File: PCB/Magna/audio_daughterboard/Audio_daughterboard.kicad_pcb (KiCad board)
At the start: 4 copper layers, 90 x 155 mm, 466 parts, among them J101 Conn_02x15_Odd_Even, J102 Conn_02x05_Odd_Even, J1301 Conn_01x03_Pin, J1302 Conn_ARM_SWD_TagConnect_TC2030, J1303 Conn_01x02_Pin, J1304 Conn_01x02_Pin, J201 PSG01550, J301 PSG01550, J601 PSG01550, Q601 NMOS, Q602 NMOS, U1001 NE5532, U1002 NE5532, U1003 NE5532, U1004 NE5532, U1005 LM1971M, U101 CY2305SXC-1HT, U102 CY2305SXC-1HT, U1101 NE5532, U1102 NE5532, U1103 NE5532, U1104 NE5532, U1105 LM1971M, U1201 NE5532, U1202 NE5532, U1203 NE5532, U1204 NE5532, U1205 LM1971M, U1301 STM32F030C8Tx, U201 WM8782SEDS, U301 WM8782SEDS, U401 PCM1789, U402 NE5532, U403 NE5532, U501 PCM1789, U502 NE5532, U503 NE5532, U601 NE5532, U701 NE5532, U801 TLV61046ADBVR, U802 LM350_TO263-3, U803 LM350_TO263-3, U901 NE5532, U902 NE5532, U903 NE5532, U904 NE5532, U905 LM1971M

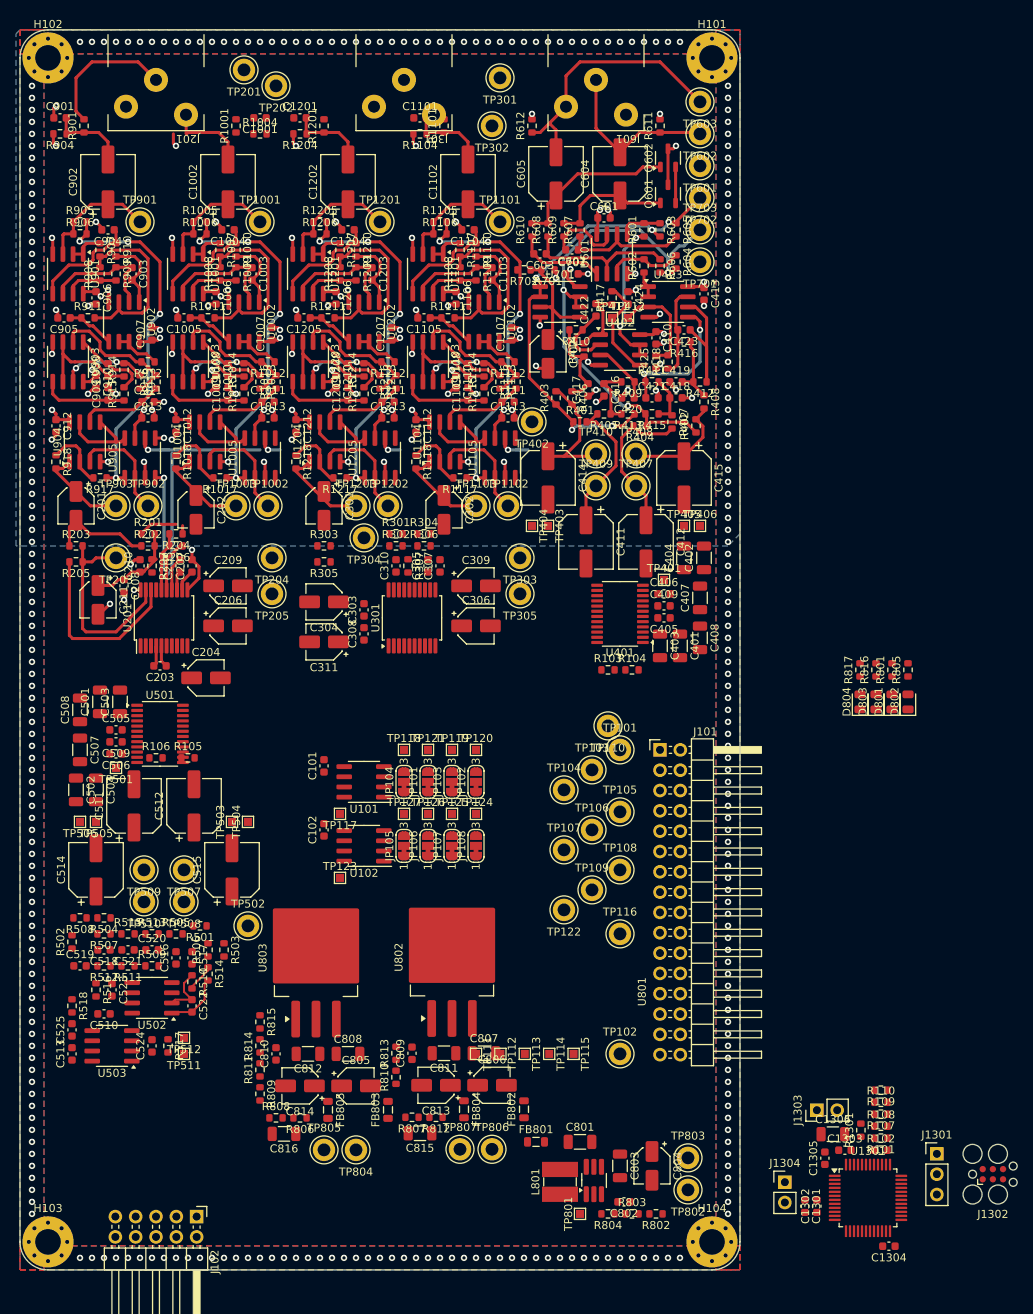
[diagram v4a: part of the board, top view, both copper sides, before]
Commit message: Finished first round of routing for the Audio Daughterboard
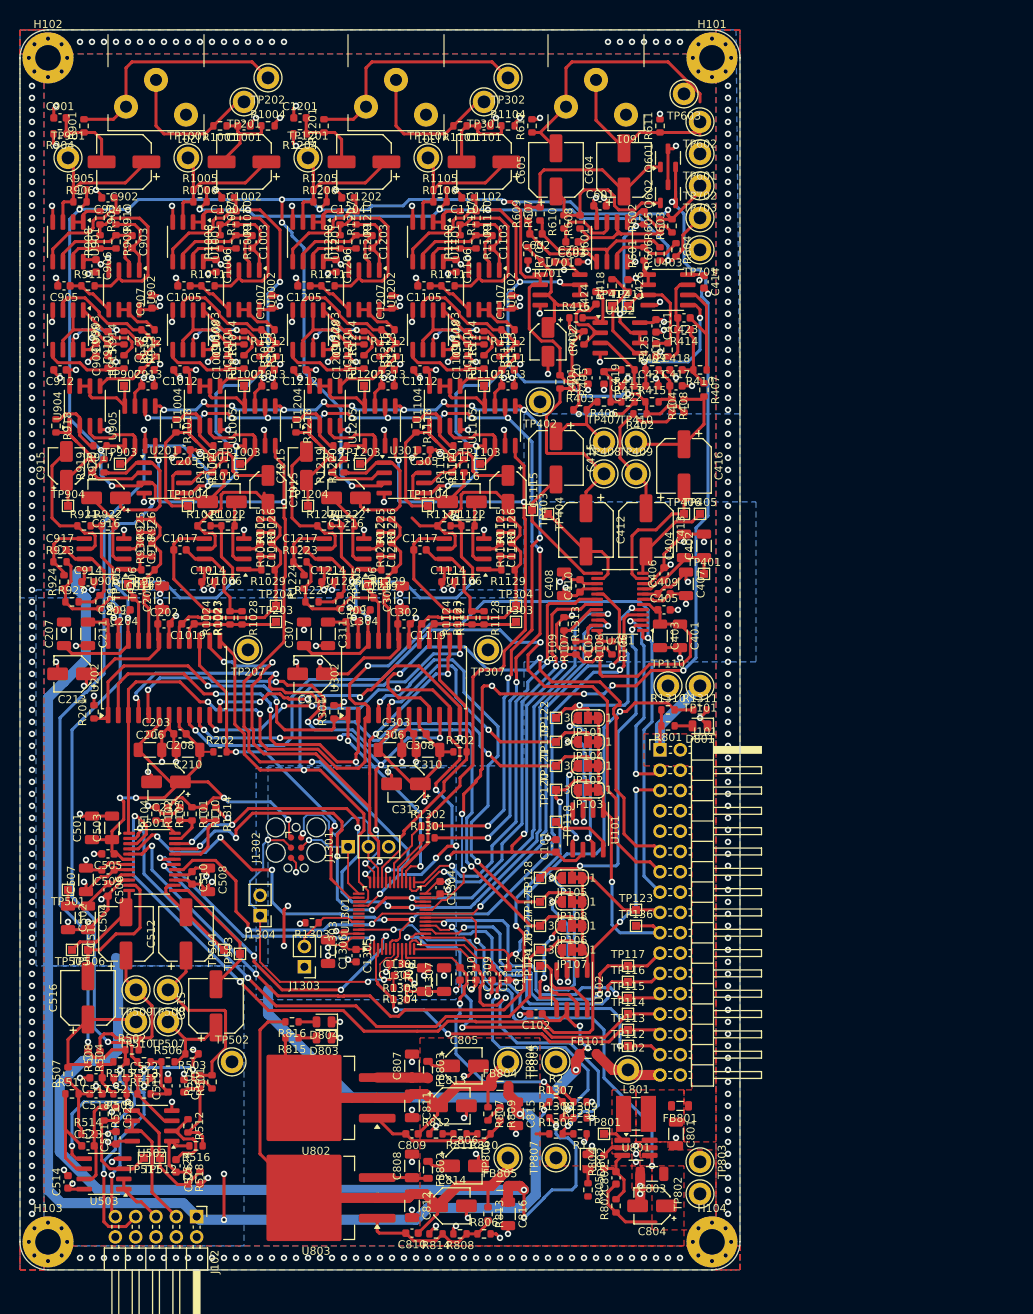
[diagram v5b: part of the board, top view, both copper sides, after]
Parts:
- removed the FB805 at (38.5, 135.0)
- removed R203, R204, R205, R206, R303, R304, R305, R306: 1k, Resistor_SMD:R_0603_1608Metric
- removed R207, R307: 2k15, Resistor_SMD:R_0603_1608Metric
- removed R803: 22k, Resistor_SMD:R_0603_1608Metric
- removed the R808 at (32.0, 136.0)
- removed the R809 at (30.0, 133.0)
- removed the R815 at (30.0, 124.0)
- removed TP103, TP104, TP105, TP106, TP107, TP108, TP109: TestPoint, TestPoint:TestPoint_Keystone_5005-5009_Compact
- removed the TP116 at (75.0, 113.0)
- removed the TP122 at (68.0, 110.0)
- added C1014: 100nF, Capacitor_SMD:C_0603_1608Metric, F.Cu at (23.5, 69.0)
- added C1015: 10uF, Capacitor_SMD:CP_Elec_4x5.8, F.Cu at (31.0, 57.5)
- added C1016: 10uF, Capacitor_SMD:CP_Elec_4x5.8, F.Cu at (25.2, 59.0)
- added C1017: 470p, Capacitor_SMD:C_0603_1608Metric, F.Cu at (20.0, 65.0)
- added C1018: 470p, Capacitor_SMD:C_0603_1608Metric, F.Cu at (30.0, 65.0)
- added C1019: 2.7n, Capacitor_SMD:C_0603_1608Metric, F.Cu at (21.0, 74.2)
- added C1114: 100nF, Capacitor_SMD:C_0603_1608Metric, F.Cu at (53.5, 69.0)
- added C1115: 10uF, Capacitor_SMD:CP_Elec_4x5.8, F.Cu at (61.0, 57.5)
- added C1116: 10uF, Capacitor_SMD:CP_Elec_4x5.8, F.Cu at (55.2, 59.0)
- added C1117: 470p, Capacitor_SMD:C_0603_1608Metric, F.Cu at (50.0, 65.0)
- added C1118: 470p, Capacitor_SMD:C_0603_1608Metric, F.Cu at (60.0, 65.0)
- added C1119: 2.7n, Capacitor_SMD:C_0603_1608Metric, F.Cu at (51.0, 74.2)
- added C1214: 100nF, Capacitor_SMD:C_0603_1608Metric, F.Cu at (38.5, 69.0)
- added C1215: 10uF, Capacitor_SMD:CP_Elec_4x5.8, F.Cu at (35.8, 54.5)
- added C1216: 10uF, Capacitor_SMD:CP_Elec_4x5.8, F.Cu at (40.8, 58.5)
- added C1217: 470p, Capacitor_SMD:C_0603_1608Metric, F.Cu at (35.0, 65.0)
- added C1218: 470p, Capacitor_SMD:C_0603_1608Metric, F.Cu at (45.0, 65.0)
- added C1219: 2.7n, Capacitor_SMD:C_0603_1608Metric, F.Cu at (45.0, 71.0)
- added C1307: 4.7uF, Capacitor_SMD:C_1206_3216Metric, F.Cu at (53.0, 118.7)
- added C1308: 4.7uF, Capacitor_SMD:C_1206_3216Metric, F.Cu at (50.5, 118.7)
- added C1309: 100nF, Capacitor_SMD:C_0603_1608Metric, F.Cu at (57.0, 118.0)
- added C1310: 100nF, Capacitor_SMD:C_0603_1608Metric, F.Cu at (55.0, 118.0)
- added C1311: 100nF, Capacitor_SMD:C_0603_1608Metric, F.Cu at (59.0, 118.0)
- added C1312: 100nF, Capacitor_SMD:C_0603_1608Metric, F.Cu at (61.0, 118.0)
- added C212: 10uF, Capacitor_SMD:CP_Elec_4x5.8, F.Cu at (18.2, 94.0)
- added C213: 10uF, Capacitor_SMD:CP_Elec_4x5.8, F.Cu at (6.50, 80.5)
- added C312: 10uF, Capacitor_SMD:CP_Elec_4x5.8, F.Cu at (48.2, 94.2)
- added C313: 10uF, Capacitor_SMD:CP_Elec_4x5.8, F.Cu at (36.5, 80.5)
- added C410: 100nF, Capacitor_SMD:C_0603_1608Metric, F.Cu at (70.0, 69.5)
- added C510: 100nF, Capacitor_SMD:C_0603_1608Metric, F.Cu at (21.5, 106.0)
- added C914: 100nF, Capacitor_SMD:C_0603_1608Metric, F.Cu at (8.50, 69.0)
- added C915: 10uF, Capacitor_SMD:CP_Elec_4x5.8, F.Cu at (5.80, 54.5)
- added C916: 10uF, Capacitor_SMD:CP_Elec_4x5.8, F.Cu at (10.8, 58.5)
- added C917: 470p, Capacitor_SMD:C_0603_1608Metric, F.Cu at (5.00, 65.0)
- added C918: 470p, Capacitor_SMD:C_0603_1608Metric, F.Cu at (15.0, 65.0)
- added C919: 2.7n, Capacitor_SMD:C_0603_1608Metric, F.Cu at (15.0, 71.0)
- added FB101: FerriteBead, Inductor_SMD:L_0805_2012Metric, F.Cu at (71.0, 128.0)
- added FB804: FerriteBead, Inductor_SMD:L_0805_2012Metric, F.Cu at (60.0, 132.0)
- added R1: 2k15, Resistor_SMD:R_0603_1608Metric, F.Cu at (70.0, 138.0)
- added R1019: 1k, Resistor_SMD:R_0603_1608Metric, F.Cu at (24.0, 54.5)
- added R1020: 1k, Resistor_SMD:R_0603_1608Metric, F.Cu at (25.5, 54.5)
- added R1021: 10k, Resistor_SMD:R_0603_1608Metric, F.Cu at (23.0, 62.0)
- added R1022: 10k, Resistor_SMD:R_0603_1608Metric, F.Cu at (26.0, 62.0)
- added R1023: 10k, Resistor_SMD:R_0603_1608Metric, F.Cu at (23.2, 73.5)
- added R1024: 680R, Resistor_SMD:R_0603_1608Metric, F.Cu at (24.8, 73.5)
- added R1025: 10k, Resistor_SMD:R_0603_1608Metric, F.Cu at (31.5, 62.0)
- added R1026: 680R, Resistor_SMD:R_0603_1608Metric, F.Cu at (30.0, 62.0)
- added R1027: 100R, Resistor_SMD:R_0603_1608Metric, F.Cu at (26.2, 73.5)
- added R1028: 1k, Resistor_SMD:R_0603_1608Metric, F.Cu at (27.8, 73.5)
- added R1029: 100R, Resistor_SMD:R_0603_1608Metric, F.Cu at (31.0, 67.5)
- added R1030: 1k, Resistor_SMD:R_0603_1608Metric, F.Cu at (31.5, 65.0)
- added R1119: 1k, Resistor_SMD:R_0603_1608Metric, F.Cu at (54.0, 54.5)
- added R1120: 1k, Resistor_SMD:R_0603_1608Metric, F.Cu at (55.5, 54.5)
- added R1121: 10k, Resistor_SMD:R_0603_1608Metric, F.Cu at (53.0, 62.0)
- added R1122: 10k, Resistor_SMD:R_0603_1608Metric, F.Cu at (56.0, 62.0)
- added R1123: 10k, Resistor_SMD:R_0603_1608Metric, F.Cu at (53.2, 73.5)
- added R1124: 680R, Resistor_SMD:R_0603_1608Metric, F.Cu at (54.8, 73.5)
- added R1125: 10k, Resistor_SMD:R_0603_1608Metric, F.Cu at (61.5, 62.0)
- added R1126: 680R, Resistor_SMD:R_0603_1608Metric, F.Cu at (60.0, 62.0)
- added R1127: 100R, Resistor_SMD:R_0603_1608Metric, F.Cu at (56.5, 73.5)
- added R1128: 1k, Resistor_SMD:R_0603_1608Metric, F.Cu at (58.0, 73.5)
- added R1129: 100R, Resistor_SMD:R_0603_1608Metric, F.Cu at (61.0, 67.5)
- added R1130: 1k, Resistor_SMD:R_0603_1608Metric, F.Cu at (61.5, 65.0)
- added R1219: 1k, Resistor_SMD:R_0603_1608Metric, F.Cu at (39.0, 54.5)
- added R1220: 1k, Resistor_SMD:R_0603_1608Metric, F.Cu at (40.5, 54.5)
- added R1221: 10k, Resistor_SMD:R_0603_1608Metric, F.Cu at (38.0, 62.0)
- added R1222: 10k, Resistor_SMD:R_0603_1608Metric, F.Cu at (41.0, 62.0)
- added R1223: 10k, Resistor_SMD:R_0603_1608Metric, F.Cu at (35.0, 66.5)
- added R1224: 680R, Resistor_SMD:R_0603_1608Metric, F.Cu at (35.5, 69.0)
- added R1225: 10k, Resistor_SMD:R_0603_1608Metric, F.Cu at (46.5, 62.0)
- added R1226: 680R, Resistor_SMD:R_0603_1608Metric, F.Cu at (45.0, 62.0)
- added R1227: 100R, Resistor_SMD:R_0603_1608Metric, F.Cu at (36.5, 71.5)
- added R1228: 1k, Resistor_SMD:R_0603_1608Metric, F.Cu at (40.0, 71.5)
- added R1229: 100R, Resistor_SMD:R_0603_1608Metric, F.Cu at (46.0, 67.5)
- added R1230: 1k, Resistor_SMD:R_0603_1608Metric, F.Cu at (46.5, 65.0)
- added R1231: 1k, Resistor_SMD:R_0603_1608Metric, F.Cu at (70.0, 134.0)
- added R1301: 68R, Resistor_SMD:R_0603_1608Metric, F.Cu at (51.0, 101.0)
- added R1302: 68R, Resistor_SMD:R_0603_1608Metric, F.Cu at (51.0, 99.5)
- added R1304: 10k, Resistor_SMD:R_0603_1608Metric, F.Cu at (47.5, 119.7)
- added R1305: 10k, Resistor_SMD:R_0603_1608Metric, F.Cu at (47.5, 121.2)
- added R1306: 10k, Resistor_SMD:R_0603_1608Metric, F.Cu at (67.0, 138.0)
- added R1307: 10k, Resistor_SMD:R_0603_1608Metric, F.Cu at (67.0, 134.0)
- added R1308: 10k, Resistor_SMD:R_0603_1608Metric, F.Cu at (67.0, 136.0)
- added R1309: 10k, Resistor_SMD:R_0603_1608Metric, F.Cu at (70.0, 136.0)
- added R1310: 10k, Resistor_SMD:R_0603_1608Metric, F.Cu at (81.0, 85.0)
- added R1311: 10k, Resistor_SMD:R_0603_1608Metric, F.Cu at (85.0, 85.0)
- added R1313: 68R, Resistor_SMD:R_0603_1608Metric, F.Cu at (68.0, 74.2)
- added R1314: 68R, Resistor_SMD:R_0603_1608Metric, F.Cu at (24.5, 98.0)
- added R2: 1k96, Resistor_SMD:R_0603_1608Metric, F.Cu at (67.0, 132.5)
- added R811: 1k96, Resistor_SMD:R_0603_1608Metric, F.Cu at (55.0, 138.0)
- added R812: 1k, Resistor_SMD:R_0603_1608Metric, F.Cu at (52.0, 138.0)
- added R919: 1k, Resistor_SMD:R_0603_1608Metric, F.Cu at (9.00, 54.5)
- added R920: 1k, Resistor_SMD:R_0603_1608Metric, F.Cu at (10.5, 54.5)
- added R921: 10k, Resistor_SMD:R_0603_1608Metric, F.Cu at (8.00, 62.0)
- added R922: 10k, Resistor_SMD:R_0603_1608Metric, F.Cu at (11.0, 62.0)
- added R923: 10k, Resistor_SMD:R_0603_1608Metric, F.Cu at (5.00, 66.5)
- added R924: 680R, Resistor_SMD:R_0603_1608Metric, F.Cu at (5.50, 69.0)
- added R925: 10k, Resistor_SMD:R_0603_1608Metric, F.Cu at (16.5, 62.0)
- added R926: 680R, Resistor_SMD:R_0603_1608Metric, F.Cu at (15.0, 62.0)
- added R927: 100R, Resistor_SMD:R_0603_1608Metric, F.Cu at (6.50, 71.5)
- added R928: 1k, Resistor_SMD:R_0603_1608Metric, F.Cu at (10.0, 71.5)
- added R929: 100R, Resistor_SMD:R_0603_1608Metric, F.Cu at (16.0, 67.5)
- added R930: 1k, Resistor_SMD:R_0603_1608Metric, F.Cu at (16.5, 65.0)
- added TP1004: TestPoint, TestPoint:TestPoint_Pad_1.0x1.0mm, F.Cu at (21.0, 59.5)
- added TP1104: TestPoint, TestPoint:TestPoint_Pad_1.0x1.0mm, F.Cu at (51.0, 59.5)
- added TP112: TestPoint, TestPoint:TestPoint_Pad_1.0x1.0mm, F.Cu at (76.0, 127.0)
- added TP1204: TestPoint, TestPoint:TestPoint_Pad_1.0x1.0mm, F.Cu at (36.0, 59.5)
- added TP123: TestPoint, TestPoint:TestPoint_Pad_1.0x1.0mm, F.Cu at (77.0, 110.0)
- added TP136: TestPoint, TestPoint:TestPoint_Pad_1.0x1.0mm, F.Cu at (77.0, 112.0)
- added TP205: TestPoint, TestPoint:TestPoint_Pad_1.0x1.0mm, F.Cu at (13.5, 69.2)
- added TP206: TestPoint, TestPoint:TestPoint_Pad_1.0x1.0mm, F.Cu at (15.5, 69.2)
- added TP305: TestPoint, TestPoint:TestPoint_Pad_1.0x1.0mm, F.Cu at (43.5, 69.2)
- added TP306: TestPoint, TestPoint:TestPoint_Pad_1.0x1.0mm, F.Cu at (45.5, 69.2)
- added TP904: TestPoint, TestPoint:TestPoint_Pad_1.0x1.0mm, F.Cu at (6.00, 59.5)
- added U1006: NE5532, Package_SO:SOIC-8_3.9x4.9mm_P1.27mm, F.Cu at (25.5, 65.5)
- added U1106: NE5532, Package_SO:SOIC-8_3.9x4.9mm_P1.27mm, F.Cu at (55.5, 65.5)
- added U1206: NE5532, Package_SO:SOIC-8_3.9x4.9mm_P1.27mm, F.Cu at (40.5, 65.5)
- added U202: CS5361, Package_SO:SOIC-24W_7.5x15.4mm_P1.27mm, F.Cu at (18.0, 81.0)
- added U302: CS5361, Package_SO:SOIC-24W_7.5x15.4mm_P1.27mm, F.Cu at (48.0, 81.0)
- added U906: NE5532, Package_SO:SOIC-8_3.9x4.9mm_P1.27mm, F.Cu at (10.5, 65.5)
- C201, C206, C211, C301, C306, C311: value 10uF -> 4.7uF; footprint Capacitor_SMD:CP_Elec_4x5.8 -> Capacitor_SMD:C_1206_3216Metric
- C202, C204, C209, C302, C304, C309: value 10uF -> 100nF; footprint Capacitor_SMD:CP_Elec_4x5.8 -> Capacitor_SMD:C_0603_1608Metric
- C207, C210, C307, C310: value 100nF -> 4.7uF; footprint Capacitor_SMD:C_0603_1608Metric -> Capacitor_SMD:C_1206_3216Metric
- J101: footprint Connector_PinHeader_2.54mm:PinHeader_2x16_P2.54mm_Horizontal -> Connector_PinHeader_2.54mm:PinHeader_2x17_P2.54mm_Horizontal
- R201, R202, R301, R302: value 100k -> 10k
- TP1002, TP1003, TP1102, TP1103, TP1202, TP1203, TP203, TP204, TP303, TP304, TP902, TP903: footprint TestPoint:TestPoint_Keystone_5005-5009_Compact -> TestPoint:TestPoint_Pad_1.0x1.0mm
- U201, U301: value WM8782SEDS -> NE5532; footprint Package_SO:SSOP-20_5.3x7.2mm_P0.65mm -> Package_SO:SOIC-8_3.9x4.9mm_P1.27mm
- moved R102 97.2 mm to (20.0, 98.0), turned to 90 degrees
- moved J1302 96.2 mm to (34.5, 102.2), turned to -90 degrees
- moved R101 95.2 mm to (21.5, 98.0), turned to -90 degrees
- moved R110 92.0 mm to (23.0, 98.0), turned to -90 degrees
- moved R816 85.2 mm to (34.0, 124.0), turned to 180 degrees
- moved R815 84.6 mm to (34.0, 126.0), turned to 180 degrees
- moved J1301 83.0 mm to (41.0, 102.1), turned to 90 degrees
- moved D804 79.8 mm to (38.0, 124.0), turned to 180 degrees
- moved D803 79.1 mm to (38.0, 126.0), turned to 180 degrees
- moved R805 76.3 mm to (71.0, 145.0), turned to -90 degrees
- moved J1304 73.6 mm to (30.0, 110.7), turned to 180 degrees
- moved R1303 73.3 mm to (36.5, 111.6), turned to 180 degrees
- moved C1304 71.8 mm to (52.5, 107.2), turned to -90 degrees
- moved R108 70.1 mm to (71.0, 77.2), turned to -90 degrees
- moved D802 70.0 mm to (71.0, 141.5), turned to -90 degrees
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- renumbered C410 to C411, C411 to C412, C412 to C413, C413 to C414, C414 to C415, C415 to C416, C416 to C417, C417 to C418, C418 to C419, C419 to C420, C420 to C421, C421 to C422, C422 to C423, C423 to C424, C424 to C425, C425 to C426, C510 to C511, C511 to C512, C512 to C513, C513 to C514, C514 to C515, C515 to C516, C516 to C517, C517 to C518, C518 to C519, C519 to C520, C520 to C521, C521 to C522, C522 to C523, C523 to C524, C524 to C525, C525 to C526, C808 to C807, C807 to C808, C810 to C809, C809 to C810, C812 to C811, C811 to C812, C814 to C813, C813 to C814, C816 to C815, C815 to C816, D804 to D803, D803 to D804, FB804 to FB805, R1301 to R1303, R807 to R806, R806 to R807, R810 to R808, R811 to R809, R814 to R810, R812 to R813, R813 to R814, R817 to R815, TP111 to TP113, TP112 to TP114, TP113 to TP115, TP114 to TP116, TP115 to TP117, TP117 to TP118, TP118 to TP119, TP119 to TP120, TP120 to TP121, TP121 to TP122, TP123 to TP124, TP124 to TP125, TP125 to TP126, TP126 to TP127, TP127 to TP128, TP205 to TP207, TP305 to TP307, U403 to U402, U402 to U403, U503 to U502, U502 to U503, U803 to U802, U802 to U803
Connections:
- net /AudioPower/14.5VAA renamed /AudioPower/12VAA
- net /AudioPower/16V renamed 14V
- C1008 pad 1: Net-(U1003A-+) -> Net-(U1003A--)
- C1011 pad 1: Net-(U1004B--) -> Net-(U1004B-+)
- C1108 pad 1: Net-(U1103A-+) -> Net-(U1103A--)
- C1111 pad 1: Net-(U1104B--) -> Net-(U1104B-+)
- C1208 pad 1: Net-(U1203A-+) -> Net-(U1203A--)
- C1211 pad 1: Net-(U1204B--) -> Net-(U1204B-+)
- C1301 pad 1: /CFG_AUDIO_ENA -> /Config MCU/MCU_NRST
- C201 pad 1: /AudioAdc0/Input Filtering/signal_out -> +5VA
- C201 pad 2: Net-(C201-Pad2) -> GND
- C202 pad 1: /AudioAdc0/Input Filtering1/signal_out -> +5VA
- C202 pad 2: Net-(C202-Pad2) -> GND
- C204 pad 1: VDD -> /AudioAdc0/VQ
- C205 pad 1: +5VA -> VAA
- C206 pad 1: +5VA -> VDD
- C207 pad 1: Net-(U201-VREFP) -> /AudioAdc0/VQ
- C208 pad 1: /AudioAdc0/VMID -> VDD
- C209 pad 1: Net-(U201-VREFP) -> Net-(U202-FILT+)
- C210 pad 1: /AudioAdc0/VMID -> VDD
- C211 pad 1: /AudioAdc0/VMID -> Net-(U202-FILT+)
- C301 pad 1: /AudioAdc1/Input Filtering/signal_out -> +5VA
- C301 pad 2: Net-(C301-Pad2) -> GND
- C302 pad 1: /AudioAdc1/Input Filtering1/signal_out -> +5VA
- C302 pad 2: Net-(C302-Pad2) -> GND
- C304 pad 1: VDD -> /AudioAdc1/VQ
- C305 pad 1: +5VA -> VAA
- C306 pad 1: +5VA -> VDD
- C307 pad 1: Net-(U301-VREFP) -> /AudioAdc1/VQ
- C308 pad 1: /AudioAdc1/VMID -> VDD
- C309 pad 1: Net-(U301-VREFP) -> Net-(U302-FILT+)
- C310 pad 1: /AudioAdc1/VMID -> VDD
- C311 pad 1: /AudioAdc1/VMID -> Net-(U302-FILT+)
- C412 pad 1: /AudioDac0/VOUTL+_BIASED -> /AudioDac0/VOUTR-_BIASED
- C412 pad 2: /AudioDac0/VOUTL+ -> /AudioDac0/VOUTR-
- C413 pad 1: /AudioDac0/VOUTR+_BIASED -> /AudioDac0/VOUTL+_BIASED
- C413 pad 2: /AudioDac0/VOUTR+ -> /AudioDac0/VOUTL+
- C415 pad 1: /AudioDac0/VOUTL-_BIASED -> /AudioDac0/VOUTR+_BIASED
- C415 pad 2: /AudioDac0/VOUTL- -> /AudioDac0/VOUTR+
- C416 pad 1: /AudioDac0/VOUTR-_BIASED -> /AudioDac0/VOUTL-_BIASED
- C416 pad 2: /AudioDac0/VOUTR- -> /AudioDac0/VOUTL-
- C417 pad 1: Net-(C416-Pad1) -> Net-(C417-Pad1)
- C418 pad 2: Net-(C417-Pad2) -> Net-(C418-Pad2)
- C419 pad 1: Net-(C418-Pad1) -> Net-(C419-Pad1)
- C420 pad 2: Net-(C419-Pad2) -> Net-(C420-Pad2)
- C421 pad 1: Net-(U402A-+) -> Net-(U403B-+)
- C422 pad 1: Net-(U403B-+) -> Net-(U402A-+)
- C423 pad 1: Net-(U402A--) -> Net-(U403B--)
- C423 pad 2: Net-(C422-Pad2) -> Net-(C423-Pad2)
- C424 pad 1: Net-(U403B--) -> Net-(U402A--)
- C424 pad 2: Net-(C423-Pad2) -> Net-(C424-Pad2)
- C512 pad 1: /AudioDac1/VOUTL+_BIASED -> /AudioDac1/VOUTR-_BIASED
- C512 pad 2: /AudioDac1/VOUTL+ -> /AudioDac1/VOUTR-
- C513 pad 1: /AudioDac1/VOUTR+_BIASED -> /AudioDac1/VOUTL+_BIASED
- C513 pad 2: /AudioDac1/VOUTR+ -> /AudioDac1/VOUTL+
- C515 pad 1: /AudioDac1/VOUTL-_BIASED -> /AudioDac1/VOUTR+_BIASED
- C515 pad 2: /AudioDac1/VOUTL- -> /AudioDac1/VOUTR+
- C516 pad 1: /AudioDac1/VOUTR-_BIASED -> /AudioDac1/VOUTL-_BIASED
- C516 pad 2: /AudioDac1/VOUTR- -> /AudioDac1/VOUTL-
- C517 pad 1: Net-(C516-Pad1) -> Net-(C517-Pad1)
- C518 pad 2: Net-(C517-Pad2) -> Net-(C518-Pad2)
- C519 pad 1: Net-(C518-Pad1) -> Net-(C519-Pad1)
- C520 pad 2: Net-(C519-Pad2) -> Net-(C520-Pad2)
- C521 pad 1: Net-(U502A-+) -> Net-(U503B-+)
- C522 pad 1: Net-(U503B-+) -> Net-(U502A-+)
- C523 pad 1: Net-(U502A--) -> Net-(U503B--)
- C523 pad 2: Net-(C522-Pad2) -> Net-(C523-Pad2)
- C524 pad 1: Net-(U503B--) -> Net-(U502A--)
- C524 pad 2: Net-(C523-Pad2) -> Net-(C524-Pad2)
- C602 pad 1: Net-(U601B--) -> Net-(U601A--)
- C603 pad 1: Net-(U601A--) -> Net-(U601B--)
- C908 pad 1: Net-(U903A-+) -> Net-(U903A--)
- C911 pad 1: Net-(U904B--) -> Net-(U904B-+)
- J101 pad 31: VDD -> /AUDIO_CFG_INT
- J102 pad 3: /AudioDac1/OUT_L -> /AudioDac1/OUT_R
- J102 pad 5: /AudioDac1/OUT_R -> /AudioDac1/OUT_L
- J1302 pad 3: /CFG_AUDIO_ENA -> /Config MCU/MCU_NRST
- J1304 pad 1: /CFG_AUDIO_ENA -> /Config MCU/MCU_NRST
- J201 pad 1: /AudioAdc0/Input Filtering/signal in -> /AudioAdc0/Input Filtering1/signal in
- J201 pad 2: /AudioAdc0/Input Filtering1/signal in -> /AudioAdc0/Input Filtering/signal in
- J301 pad 1: /AudioAdc1/Input Filtering/signal in -> /AudioAdc1/Input Filtering1/signal in
- J301 pad 2: /AudioAdc1/Input Filtering1/signal in -> /AudioAdc1/Input Filtering/signal in
- JP102 pad 2: /DAC0_MCLK -> /ADC0_MCLK
- JP103 pad 2: /ADC1_MCLK -> /DAC0_MCLK
- JP104 pad 2: /ADC0_MCLK -> /ADC1_MCLK
- JP106 pad 2: /DAC0_BCLK -> /ADC0_BCLK
- JP107 pad 2: /ADC1_BCLK -> /DAC0_BCLK
- JP108 pad 2: /ADC0_BCLK -> /ADC1_BCLK
- Q601 pad 2: MASTER_MUTE -> /Config MCU/LINE_MUTE
- Q602 pad 2: MASTER_MUTE -> /Config MCU/LINE_MUTE
- R1005 pad 2: VAA_BIAS_R -> VAA_BIAS_L
- R1006 pad 2: VAA_BIAS_R -> VAA_BIAS_L
- R1012 pad 2: Net-(U1003A--) -> Net-(U1003A-+)
- R1013 pad 2: Net-(U1003A--) -> Net-(U1003A-+)
- R1014 pad 1: Net-(U1003A-+) -> Net-(U1003A--)
- R1016 pad 1: Net-(U1004B--) -> Net-(U1004B-+)
- R1016 pad 2: Net-(U1003A--) -> Net-(U1003A-+)
- R1017 pad 1: VAA_BIAS_R -> VAA_BIAS_L
- R1018 pad 2: /AudioAdc0/Input Filtering1/signal_out -> Net-(C1015-Pad1)
- R110 pad 1: /AudioDac0/MODE -> VDD
- R110 pad 2: GND -> /AudioDac1/MODE
- R1105 pad 2: VAA_BIAS_R -> VAA_BIAS_L
- R1106 pad 2: VAA_BIAS_R -> VAA_BIAS_L
- R1112 pad 2: Net-(U1103A--) -> Net-(U1103A-+)
- R1113 pad 2: Net-(U1103A--) -> Net-(U1103A-+)
- R1114 pad 1: Net-(U1103A-+) -> Net-(U1103A--)
- R1116 pad 1: Net-(U1104B--) -> Net-(U1104B-+)
- R1116 pad 2: Net-(U1103A--) -> Net-(U1103A-+)
- R1117 pad 1: VAA_BIAS_R -> VAA_BIAS_L
- R1118 pad 2: /AudioAdc1/Input Filtering1/signal_out -> Net-(C1115-Pad1)
- R1205 pad 2: VAA_BIAS_L -> VAA_BIAS_R
- R1206 pad 2: VAA_BIAS_L -> VAA_BIAS_R
- R1212 pad 2: Net-(U1203A--) -> Net-(U1203A-+)
- R1213 pad 2: Net-(U1203A--) -> Net-(U1203A-+)
- R1214 pad 1: Net-(U1203A-+) -> Net-(U1203A--)
- R1216 pad 1: Net-(U1204B--) -> Net-(U1204B-+)
- R1216 pad 2: Net-(U1203A--) -> Net-(U1203A-+)
- R1217 pad 1: VAA_BIAS_L -> VAA_BIAS_R
- R1218 pad 2: /AudioAdc1/Input Filtering/signal_out -> Net-(C1215-Pad1)
- R201 pad 1: Net-(C202-Pad2) -> /AudioAdc0/ADC_RST
- R201 pad 2: /AudioAdc0/VMID -> GND
- R202 pad 1: Net-(C201-Pad2) -> VDD
- R202 pad 2: /AudioAdc0/VMID -> /AudioAdc0/ADC_OVFL
- R301 pad 1: Net-(C302-Pad2) -> /AudioAdc0/ADC_RST
- R301 pad 2: /AudioAdc1/VMID -> GND
- R302 pad 1: Net-(C301-Pad2) -> VDD
- R302 pad 2: /AudioAdc1/VMID -> /AudioAdc1/ADC_OVFL
- R401 pad 1: VAA_BIAS_L -> VAA_BIAS_R
- R401 pad 2: /AudioDac0/VOUTL+_BIASED -> /AudioDac0/VOUTR-_BIASED
- R402 pad 1: VAA_BIAS_R -> VAA_BIAS_L
- R402 pad 2: /AudioDac0/VOUTR-_BIASED -> /AudioDac0/VOUTL+_BIASED
- R403 pad 1: VAA_BIAS_L -> VAA_BIAS_R
- R403 pad 2: /AudioDac0/VOUTL-_BIASED -> /AudioDac0/VOUTR+_BIASED
- R404 pad 1: VAA_BIAS_R -> VAA_BIAS_L
- R404 pad 2: /AudioDac0/VOUTR+_BIASED -> /AudioDac0/VOUTL-_BIASED
- R405 pad 1: Net-(C416-Pad1) -> Net-(C420-Pad2)
- R405 pad 2: /AudioDac0/VOUTL+_BIASED -> /AudioDac0/VOUTR-_BIASED
- R406 pad 1: Net-(C417-Pad2) -> Net-(C419-Pad1)
- R406 pad 2: /AudioDac0/VOUTL-_BIASED -> /AudioDac0/VOUTR+_BIASED
- R407 pad 1: Net-(C418-Pad1) -> Net-(C418-Pad2)
- R407 pad 2: /AudioDac0/VOUTR+_BIASED -> /AudioDac0/VOUTL-_BIASED
- R408 pad 1: Net-(C419-Pad2) -> Net-(C417-Pad1)
- R408 pad 2: /AudioDac0/VOUTR-_BIASED -> /AudioDac0/VOUTL+_BIASED
- R409 pad 1: Net-(U402A-+) -> Net-(U403B-+)
- R409 pad 2: Net-(C416-Pad1) -> Net-(C417-Pad1)
- R410 pad 1: Net-(U402A--) -> Net-(U403B--)
- R410 pad 2: Net-(C417-Pad2) -> Net-(C418-Pad2)
- R411 pad 1: Net-(U403B-+) -> Net-(U402A-+)
- R411 pad 2: Net-(C418-Pad1) -> Net-(C419-Pad1)
- R412 pad 1: Net-(U403B--) -> Net-(U402A--)
- R412 pad 2: Net-(C419-Pad2) -> Net-(C420-Pad2)
- R413 pad 1: VAA_BIAS_L -> Net-(C419-Pad1)
- R413 pad 2: Net-(C416-Pad1) -> VAA_BIAS_R
- R414 pad 1: Net-(C417-Pad2) -> Net-(C418-Pad2)
- R414 pad 2: Net-(C422-Pad2) -> Net-(C423-Pad2)
- R415 pad 1: Net-(C418-Pad1) -> VAA_BIAS_L
- R415 pad 2: VAA_BIAS_R -> Net-(C417-Pad1)
- R416 pad 1: Net-(C419-Pad2) -> Net-(C420-Pad2)
- R416 pad 2: Net-(C423-Pad2) -> Net-(C424-Pad2)
- R417 pad 1: Net-(C422-Pad2) -> Net-(C423-Pad2)
- R418 pad 1: Net-(C423-Pad2) -> Net-(C424-Pad2)
- R501 pad 1: VAA_BIAS_L -> VAA_BIAS_R
- R501 pad 2: /AudioDac1/VOUTL+_BIASED -> /AudioDac1/VOUTR-_BIASED
- R502 pad 1: VAA_BIAS_R -> VAA_BIAS_L
- R502 pad 2: /AudioDac1/VOUTR-_BIASED -> /AudioDac1/VOUTL+_BIASED
- R503 pad 1: VAA_BIAS_L -> VAA_BIAS_R
- R503 pad 2: /AudioDac1/VOUTL-_BIASED -> /AudioDac1/VOUTR+_BIASED
- R504 pad 1: VAA_BIAS_R -> VAA_BIAS_L
- R504 pad 2: /AudioDac1/VOUTR+_BIASED -> /AudioDac1/VOUTL-_BIASED
- R505 pad 1: Net-(C516-Pad1) -> Net-(C520-Pad2)
- R505 pad 2: /AudioDac1/VOUTL+_BIASED -> /AudioDac1/VOUTR-_BIASED
- R506 pad 1: Net-(C517-Pad2) -> Net-(C519-Pad1)
- R506 pad 2: /AudioDac1/VOUTL-_BIASED -> /AudioDac1/VOUTR+_BIASED
- R507 pad 1: Net-(C518-Pad1) -> Net-(C518-Pad2)
- R507 pad 2: /AudioDac1/VOUTR+_BIASED -> /AudioDac1/VOUTL-_BIASED
- R508 pad 1: Net-(C519-Pad2) -> Net-(C517-Pad1)
- R508 pad 2: /AudioDac1/VOUTR-_BIASED -> /AudioDac1/VOUTL+_BIASED
- R509 pad 1: Net-(U502A-+) -> Net-(U503B-+)
- R509 pad 2: Net-(C516-Pad1) -> Net-(C517-Pad1)
- R510 pad 1: Net-(U502A--) -> Net-(U503B--)
- R510 pad 2: Net-(C517-Pad2) -> Net-(C518-Pad2)
- R511 pad 1: Net-(U503B-+) -> Net-(U502A-+)
- R511 pad 2: Net-(C518-Pad1) -> Net-(C519-Pad1)
- R512 pad 1: Net-(U503B--) -> Net-(U502A--)
- R512 pad 2: Net-(C519-Pad2) -> Net-(C520-Pad2)
- R513 pad 1: VAA_BIAS_L -> Net-(C519-Pad1)
- R513 pad 2: Net-(C516-Pad1) -> VAA_BIAS_R
- R514 pad 1: Net-(C517-Pad2) -> Net-(C518-Pad2)
- R514 pad 2: Net-(C522-Pad2) -> Net-(C523-Pad2)
- R515 pad 1: Net-(C518-Pad1) -> VAA_BIAS_L
- R515 pad 2: VAA_BIAS_R -> Net-(C517-Pad1)
- R516 pad 1: Net-(C519-Pad2) -> Net-(C520-Pad2)
- R516 pad 2: Net-(C523-Pad2) -> Net-(C524-Pad2)
- R517 pad 1: Net-(C522-Pad2) -> Net-(C523-Pad2)
- R518 pad 1: Net-(C523-Pad2) -> Net-(C524-Pad2)
- R601 pad 2: Net-(U601B-+) -> Net-(U601A-+)
- R602 pad 2: Net-(U601A-+) -> Net-(U601B-+)
- R603 pad 2: VAA_BIAS_L -> VAA_BIAS_R
- R604 pad 2: VAA_BIAS_R -> VAA_BIAS_L
- R605 pad 1: VAA_BIAS_L -> Net-(U601B--)
- R605 pad 2: Net-(U601B--) -> VAA_BIAS_R
- R606 pad 1: Net-(U601A--) -> VAA_BIAS_L
- R606 pad 2: VAA_BIAS_R -> Net-(U601A--)
- R607 pad 1: Net-(U601B--) -> Net-(U601A--)
- R608 pad 1: Net-(U601A--) -> Net-(U601B--)
- R802 pad 2: Net-(R802-Pad2) -> /AudioPower/Boost Feedback
- R807 pad 2: Net-(R806-Pad2) -> Net-(R807-Pad2)
- R809 pad 1: Net-(R809-Pad1) -> Net-(R807-Pad2)
- R905 pad 2: VAA_BIAS_L -> VAA_BIAS_R
- R906 pad 2: VAA_BIAS_L -> VAA_BIAS_R
- R912 pad 2: Net-(U903A--) -> Net-(U903A-+)
- R913 pad 2: Net-(U903A--) -> Net-(U903A-+)
- R914 pad 1: Net-(U903A-+) -> Net-(U903A--)
- R916 pad 1: Net-(U904B--) -> Net-(U904B-+)
- R916 pad 2: Net-(U903A--) -> Net-(U903A-+)
- R917 pad 1: VAA_BIAS_L -> VAA_BIAS_R
- R918 pad 2: /AudioAdc0/Input Filtering/signal_out -> Net-(C915-Pad1)
- TP1002 pad 1: /AudioAdc0/Input Filtering1/antennuated_input -> /AudioAdc0/Input Filtering1/Filtered_input
- TP1003 pad 1: /AudioAdc0/Input Filtering1/signal_out -> /AudioAdc0/Input Filtering1/antennuated_input
- TP102 pad 1: VDD -> Net-(J101-Pin_33)
- TP1102 pad 1: /AudioAdc1/Input Filtering1/antennuated_input -> /AudioAdc1/Input Filtering1/Filtered_input
- TP1103 pad 1: /AudioAdc1/Input Filtering1/signal_out -> /AudioAdc1/Input Filtering1/antennuated_input
- TP119 pad 1: /ADC0_MCLK -> /ADC1_MCLK
- TP120 pad 1: /ADC1_MCLK -> /DAC0_MCLK
- TP1202 pad 1: /AudioAdc1/Input Filtering/antennuated_input -> /AudioAdc1/Input Filtering/Filtered_input
- TP1203 pad 1: /AudioAdc1/Input Filtering/signal_out -> /AudioAdc1/Input Filtering/antennuated_input
- TP121 pad 1: /DAC0_MCLK -> /ADC0_MCLK
- TP125 pad 1: /ADC0_BCLK -> /ADC1_BCLK
- TP126 pad 1: /ADC1_BCLK -> /DAC0_BCLK
- TP127 pad 1: /DAC0_BCLK -> /ADC0_BCLK
- TP201 pad 1: /AudioAdc0/Input Filtering/signal in -> /AudioAdc0/Input Filtering1/signal in
- TP202 pad 1: /AudioAdc0/Input Filtering1/signal in -> /AudioAdc0/Input Filtering/signal in
- TP203 pad 1: Net-(U201-AINL) -> /AudioAdc0/Input Filtering1/signal_out+
- TP204 pad 1: Net-(U201-AINR) -> /AudioAdc0/Input Filtering1/signal_out-
- TP301 pad 1: /AudioAdc1/Input Filtering/signal in -> /AudioAdc1/Input Filtering1/signal in
- TP302 pad 1: /AudioAdc1/Input Filtering1/signal in -> /AudioAdc1/Input Filtering/signal in
- TP303 pad 1: Net-(U301-AINL) -> /AudioAdc1/Input Filtering1/signal_out+
- TP304 pad 1: Net-(U301-AINR) -> /AudioAdc1/Input Filtering1/signal_out-
- TP902 pad 1: /AudioAdc0/Input Filtering/antennuated_input -> /AudioAdc0/Input Filtering/Filtered_input
- TP903 pad 1: /AudioAdc0/Input Filtering/signal_out -> /AudioAdc0/Input Filtering/antennuated_input
- U1003 pad 6: Net-(U1003A-+) -> Net-(U1003A--)
- U1004 pad 1: /AudioAdc0/Input Filtering1/signal_out -> Net-(C1015-Pad1)
- U1004 pad 5: /AudioAdc0/Input Filtering1/Filtered_input -> Net-(U1004B-+)
- U1004 pad 6: Net-(U1004B--) -> /AudioAdc0/Input Filtering1/Filtered_input
- U1005 pad 1: VAA_BIAS_R -> VAA_BIAS_L
- U1103 pad 6: Net-(U1103A-+) -> Net-(U1103A--)
- U1104 pad 1: /AudioAdc1/Input Filtering1/signal_out -> Net-(C1115-Pad1)
- U1104 pad 5: /AudioAdc1/Input Filtering1/Filtered_input -> Net-(U1104B-+)
- U1104 pad 6: Net-(U1104B--) -> /AudioAdc1/Input Filtering1/Filtered_input
- U1105 pad 1: VAA_BIAS_R -> VAA_BIAS_L
- U1203 pad 6: Net-(U1203A-+) -> Net-(U1203A--)
- U1204 pad 1: /AudioAdc1/Input Filtering/signal_out -> Net-(C1215-Pad1)
- U1204 pad 5: /AudioAdc1/Input Filtering/Filtered_input -> Net-(U1204B-+)
- U1204 pad 6: Net-(U1204B--) -> /AudioAdc1/Input Filtering/Filtered_input
- U1205 pad 1: VAA_BIAS_L -> VAA_BIAS_R
- U1301 pad 10: unconnected-(U1301-PA0-Pad10) -> /Config MCU/VAA_MON
- U1301 pad 11: unconnected-(U1301-PA1-Pad11) -> /Config MCU/5VA_MON
- U1301 pad 12: unconnected-(U1301-PA2-Pad12) -> /Config MCU/14V_MON
- U1301 pad 13: unconnected-(U1301-PA3-Pad13) -> /Config MCU/VIN_MON
- U1301 pad 18: unconnected-(U1301-PB0-Pad18) -> /AUDIO_CFG_INT
- U1301 pad 19: MASTER_MUTE -> /AudioDac0/MUTE
- U1301 pad 2: unconnected-(U1301-PC13-Pad2) -> /AudioDac1/ZERO2
- U1301 pad 20: /VAA_EN -> /Config MCU/LINE_MUTE
- U1301 pad 25: /ADC_FORMAT -> /AudioDac0/ZERO1
- U1301 pad 26: /ADC_M/S -> /AudioDac0/ZERO2
- U1301 pad 27: /ADC_FSAMPEN -> /AudioAdc0/ADC_RST
- U1301 pad 28: /AudioAdc0/AMP_LOAD -> /AudioAdc1/AMP_LOAD
- U1301 pad 29: /AudioAdc0/AMP_DATA -> Net-(U1301-PA8)
- U1301 pad 3: unconnected-(U1301-PC14-Pad3) -> /CFG_AUDIO_ENA
- U1301 pad 30: /AudioAdc0/AMP_CLK -> Net-(U1301-PA9)
- U1301 pad 32: /AudioAdc1/AMP_LOAD -> /AudioAdc0/AMP_LOAD
- U1301 pad 33: /ADC_IWL -> /AudioAdc1/ADC_OVFL
- U1301 pad 35: /AudioDac0/ZERO2 -> /AudioAdc0/ADC_MDIV
- U1301 pad 36: /AudioDac0/ZERO1 -> /AudioAdc0/ADC_M0
- U1301 pad 38: unconnected-(U1301-PA15-Pad38) -> /AudioAdc0/ADC_OVFL
- U1301 pad 39: /AudioDac0/~{RST} -> /AudioAdc0/ADC_M1
- U1301 pad 4: unconnected-(U1301-PC15-Pad4) -> /AudioDac1/ZERO1
- U1301 pad 40: /AudioDac1/MS/ADR0/RSV -> /AudioAdc0/ADC_HPF
- U1301 pad 41: /AudioDac0/MS/ADR0/RSV -> unconnected-(U1301-PB5-Pad41)
- U1301 pad 42: unconnected-(U1301-PB6-Pad42) -> /Config MCU/SEL_DAC0
- U1301 pad 45: /AudioDac0/MODE -> /Config MCU/MODE
- U1301 pad 46: /AudioDac0/MUTE -> /VAA_EN
- U1301 pad 5: /AudioDac1/ZERO2 -> unconnected-(U1301-PF0-Pad5)
- U1301 pad 6: /AudioDac1/ZERO1 -> /AudioDac0/~{RST}
- U1301 pad 7: /CFG_AUDIO_ENA -> /Config MCU/MCU_NRST
- U201 pad 1: /ADC0_MCLK -> /AudioAdc0/Input Filtering/INV_OUT
- U201 pad 2: /ADC_DATA_0 -> /AudioAdc0/Input Filtering/INV-
- U201 pad 3: /LRCLK -> VAA_BIAS_R
- U201 pad 5: VDD -> VAA_BIAS_L
- U201 pad 6: /ADC0_BCLK -> /AudioAdc0/Input Filtering1/INV-
- U201 pad 7: /ADC_IWL -> /AudioAdc0/Input Filtering1/INV_OUT
- U201 pad 8: /ADC_FSAMPEN -> VAA
- U301 pad 1: /ADC1_MCLK -> /AudioAdc1/Input Filtering/INV_OUT
- U301 pad 2: /ADC_DATA_1 -> /AudioAdc1/Input Filtering/INV-
- U301 pad 3: /LRCLK -> VAA_BIAS_R
- U301 pad 5: VDD -> VAA_BIAS_L
- U301 pad 6: /ADC1_BCLK -> /AudioAdc1/Input Filtering1/INV-
- U301 pad 7: /ADC_IWL -> /AudioAdc1/Input Filtering1/INV_OUT
- U301 pad 8: /ADC_FSAMPEN -> VAA
- U402 pad 1: /AudioDac0/OUT_R -> Net-(C424-Pad2)
- U402 pad 2: /AudioDac0/OUT_R -> Net-(U402A--)
- U402 pad 3: /AudioDac0/RIGHT_FILTERED -> Net-(U402A-+)
- U402 pad 5: Net-(U403B-+) -> /AudioDac0/RIGHT_FILTERED
- U402 pad 6: Net-(U403B--) -> /AudioDac0/OUT_R
- U402 pad 7: Net-(C423-Pad2) -> /AudioDac0/OUT_R
- U403 pad 1: Net-(C422-Pad2) -> /AudioDac0/OUT_L
- U403 pad 2: Net-(U402A--) -> /AudioDac0/OUT_L
- U403 pad 3: Net-(U402A-+) -> /AudioDac0/LEFT_FILTERED
- U403 pad 5: /AudioDac0/LEFT_FILTERED -> Net-(U403B-+)
- U403 pad 6: /AudioDac0/OUT_L -> Net-(U403B--)
- U403 pad 7: /AudioDac0/OUT_L -> Net-(C423-Pad2)
- U501 pad 20: /AudioDac0/MODE -> /AudioDac1/MODE
- U502 pad 1: /AudioDac1/OUT_R -> Net-(C524-Pad2)
- U502 pad 2: /AudioDac1/OUT_R -> Net-(U502A--)
- U502 pad 3: /AudioDac1/RIGHT_FILTERED -> Net-(U502A-+)
- U502 pad 5: Net-(U503B-+) -> /AudioDac1/RIGHT_FILTERED
- U502 pad 6: Net-(U503B--) -> /AudioDac1/OUT_R
- U502 pad 7: Net-(C523-Pad2) -> /AudioDac1/OUT_R
- U503 pad 1: Net-(C522-Pad2) -> /AudioDac1/OUT_L
- U503 pad 2: Net-(U502A--) -> /AudioDac1/OUT_L
- U503 pad 3: Net-(U502A-+) -> /AudioDac1/LEFT_FILTERED
- U503 pad 5: /AudioDac1/LEFT_FILTERED -> Net-(U503B-+)
- U503 pad 6: /AudioDac1/OUT_L -> Net-(U503B--)
- U503 pad 7: /AudioDac1/OUT_L -> Net-(C523-Pad2)
- U601 pad 1: /Line Driver/LINE_OUT_BUFF_R -> /Line Driver/LINE_OUT_BUFF_L
- U601 pad 7: /Line Driver/LINE_OUT_BUFF_L -> /Line Driver/LINE_OUT_BUFF_R
- U701 pad 1: VAA_BIAS_L -> VAA_BIAS_R
- U701 pad 2: VAA_BIAS_L -> VAA_BIAS_R
- U701 pad 6: VAA_BIAS_R -> VAA_BIAS_L
- U701 pad 7: VAA_BIAS_R -> VAA_BIAS_L
- U903 pad 6: Net-(U903A-+) -> Net-(U903A--)
- U904 pad 1: /AudioAdc0/Input Filtering/signal_out -> Net-(C915-Pad1)
- U904 pad 5: /AudioAdc0/Input Filtering/Filtered_input -> Net-(U904B-+)
- U904 pad 6: Net-(U904B--) -> /AudioAdc0/Input Filtering/Filtered_input
- U905 pad 1: VAA_BIAS_L -> VAA_BIAS_R
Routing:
- net VDD: track 2.75 -> 258.7 mm, vias 0 -> 16
- net GND: track 124.8 -> 345.6 mm, vias 82 -> 193
- net VAA: track 75.0 -> 268.8 mm, vias 25 -> 36
- net VAA_BIAS_L: track 149.0 -> 342.6 mm, vias 13 -> 16
- net VAA_BIAS_R: track 154.7 -> 347.2 mm, vias 11 -> 19
- net +5VA: track 2.38 -> 179.0 mm, vias 0 -> 11
- net /LRCLK: track 0.00 -> 146.6 mm, vias 0 -> 4
- net /Config MCU/LINE_MUTE: track 0.00 -> 127.4 mm, vias 0 -> 7
- net /DAC_DATA_0: track 0.00 -> 115.1 mm, vias 0 -> 4
- net /AudioAdc0/AMP_DATA: track 1.07 -> 114.9 mm, vias 1 -> 13
- net /AudioDac0/~{RST}: track 0.00 -> 108.3 mm, vias 0 -> 6
- net /AudioDac0/MD/SDA/DEMP: track 0.00 -> 99.7 mm, vias 0 -> 6
- net /AudioDac0/MC/SCL/DMT: track 0.00 -> 99.1 mm, vias 0 -> 6
- net /ADC_DATA_0: track 0.00 -> 96.4 mm, vias 0 -> 2
- net /AudioDac0/MUTE: track 0.00 -> 96.0 mm, vias 0 -> 4
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- added copper zone on F.Cu, net +5V
- added copper zone on B.Cu, net +5VA
- added copper zone on F.Cu, net /AudioPower/Boost in
- added copper zone on F.Cu, net /AudioPower/Boost_SW
- added copper zone on F.Cu, net 14V
- added copper zone on F.Cu, net GND
- added copper zone on B.Cu, net VDD
